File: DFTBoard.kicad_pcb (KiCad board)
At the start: 8 copper layers, 148.5 x 62 mm, 294 parts, among them CON1 AVR-JTAG-10, J1 PJ-102A, J2 AUDIO JACK, J3 AUDIO JACK, J4 AUDIO JACK, J5 JACK_TRS_4PINS, J6 USB_A, J7 USB_B, J8 Micro_SD_Card_Det, J9 HDMI_A, Q1 IRLML2502, Q10 IRLML2502, Q2 IRLML2502, Q3 IRLML2502, Q4 IRLML2502, Q5 IRLML2502, Q6 IRLML2502, Q7 IRLML2502, Q8 IRLML2502, Q9 IRLML2502, SW1 TL6215RF200BDT, U1 LM3880, U10 USB3320, U11 MIC2025-1YMM, U12 USB3320, U13 VL53L0X, U14 APDS-9960, U15 MT41K256M16HA-125_E, U16 MT41K256M16HA-125_E, U17 FTDITypeUART, U18 ABRACON-ASDMB, U19 S25FL256SAGNFI001, U2 LM3880, U20 xc7z020clg484, U3 SC189 - 1.0V, U4 SC189 - 3.3V, U5 TLV62080DSGx, U6 LM1085-5.0, U7 SC189 - 1.8V, U8 TPS51200DRCR, U9 TLV320AIC3104, Y1 ABM3-24.000MHZ-D2Y-T, Y2 ABM3-24.000MHZ-D2Y-T

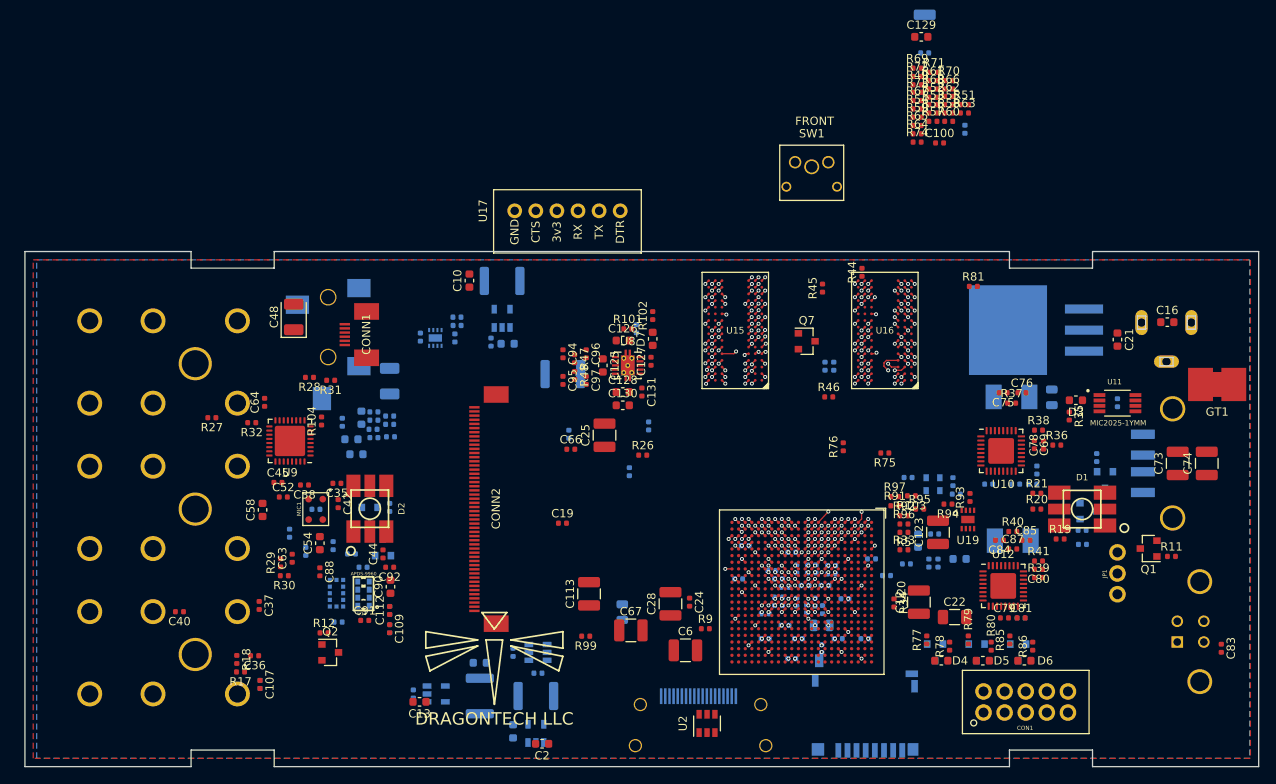
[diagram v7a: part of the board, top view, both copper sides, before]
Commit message: low 2 ddr3 bytes delay matched WRT package flight time
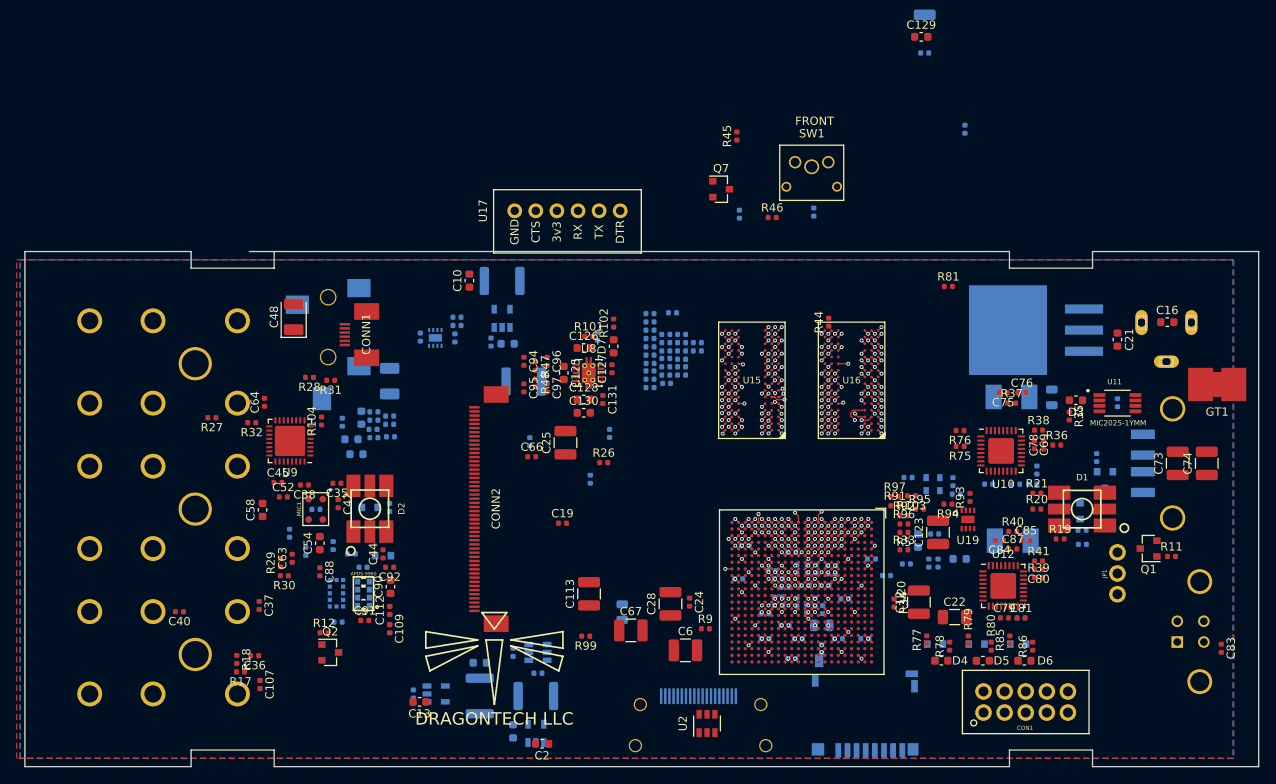
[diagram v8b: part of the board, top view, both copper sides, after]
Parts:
- C100, R49, R51, R52, R53, R54, R55, R56, R57, R58, R59, R60, R61, R62, R63, R64, R65, R66, R67, R68, R69, R70, R71, R72, R73, R74: moved to B.Cu
- moved R69 50.1 mm to (181.7, 109.4)
- moved R71 49.3 mm to (183.7, 108.9)
- moved R72 48.6 mm to (181.7, 108.4)
- moved R61 47.8 mm to (183.6, 107.9)
- moved R70 47.8 mm to (185.5, 107.9)
- moved R49 47.1 mm to (181.7, 107.4)
- moved R66 46.4 mm to (185.5, 106.9)
- moved R68 46.4 mm to (183.6, 106.9)
- moved R73 45.8 mm to (181.8, 106.5)
- moved R62 45.1 mm to (185.5, 106.0)
- moved R52 45.0 mm to (183.6, 105.9)
- moved R67 44.4 mm to (181.7, 105.5)
- moved R51 43.7 mm to (187.4, 105.0)
- moved R53 43.7 mm to (183.6, 105.0)
- moved R55 43.7 mm to (185.5, 105.0)
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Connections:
- U15 pad A2: DDR3_DQ31 -> DDR3_DQ25
- U15 pad A3: DDR3_DQ26 -> DDR3_DQ27
- U15 pad A7: DDR3_DQ28 -> DDR3_DQ26
- U15 pad C2: DDR3_DQ25 -> DDR3_DQ28
- U15 pad C3: DDR3_DQ27 -> DDR3_DQ31
- U15 pad G2: DDR3_DQ22 -> DDR3_DQ18
- U15 pad H3: DDR3_DQ18 -> DDR3_DQ22
- U16 pad E3: DDR3_DQ0 -> DDR3_DQ4
- U16 pad F7: DDR3_DQ4 -> DDR3_DQ6
- U16 pad H7: DDR3_DQ6 -> DDR3_DQ0
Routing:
- net DDR3_A11: track 81.8 -> 52.6 mm
- net DDR3_A13: track 77.0 -> 50.0 mm
- net DDR3_A9: track 75.1 -> 48.3 mm
- net DDR3_A6: track 75.2 -> 50.8 mm
- net DDR3_DRST#: track 72.2 -> 49.3 mm
- net DDR3_A7: track 72.1 -> 51.3 mm
- net DDR3_A8: track 69.9 -> 50.7 mm
- net DDR3_A2: track 70.2 -> 51.4 mm
- net DDR3_BA0: track 70.1 -> 51.3 mm
- net DDR3_DQ18: track 0.56 -> 19.1 mm, vias 1 -> 2
- net DDR3_CK_N: track 58.2 -> 40.8 mm
- net DDR3_DQ16: track 0.00 -> 17.1 mm, vias 0 -> 2
- net DDR3_A14: track 67.5 -> 50.7 mm
- net DDR3_A3: track 68.2 -> 51.4 mm
- net DDR3_A12: track 63.8 -> 47.1 mm
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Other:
- outline, holes or cut-outs redrawn
